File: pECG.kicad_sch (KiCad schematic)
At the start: 48 parts, among them J2 USB_C_Receptacle_USB2.0_14P, J4 AudioJack3, U2 SPX3819M5-L-3-3, U4 TP4065

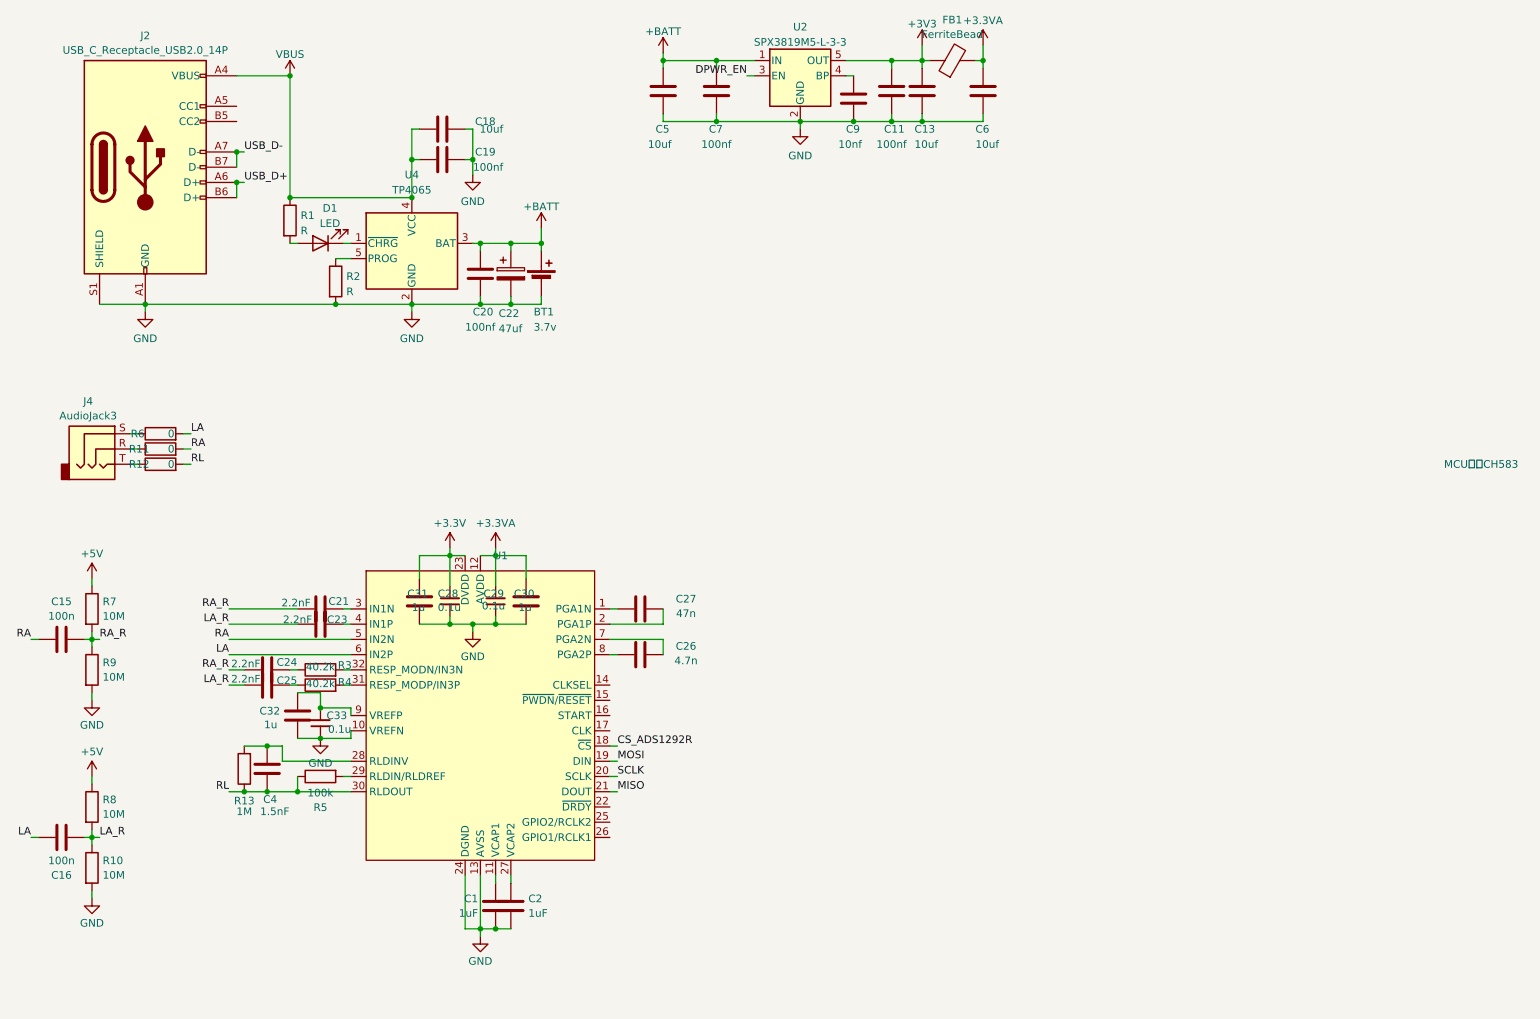
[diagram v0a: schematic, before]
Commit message: PCB部分布局和布线
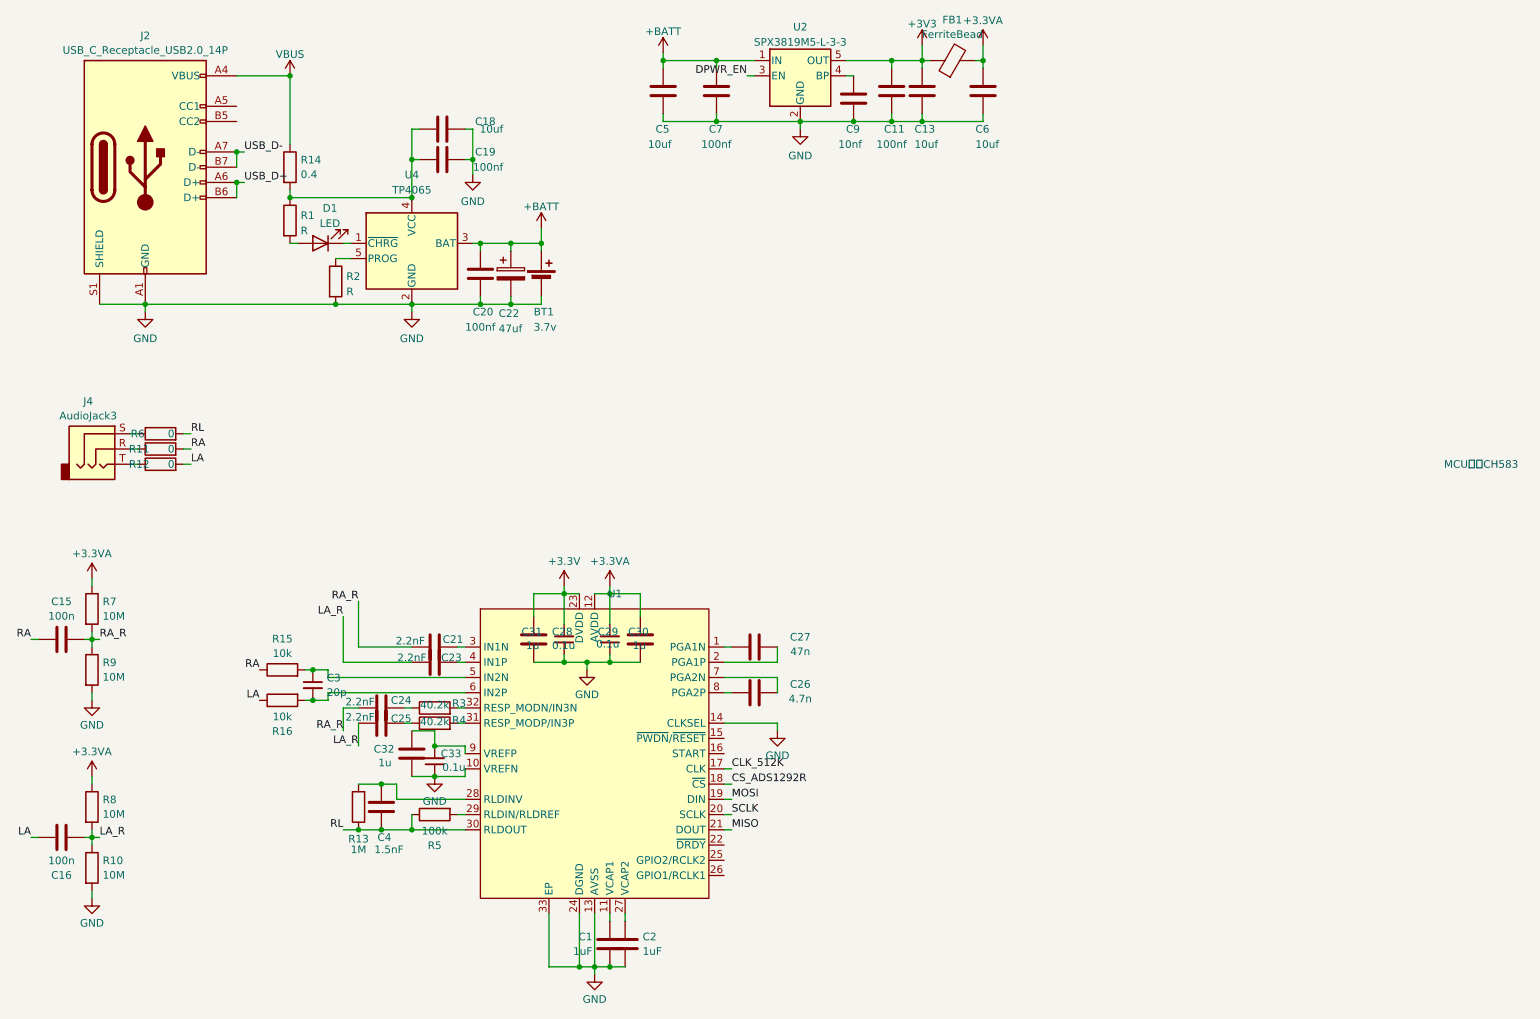
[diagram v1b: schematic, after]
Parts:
- added C3: 20p, Capacitor_SMD:C_0402_1005Metric, symbol Device:C_Small
- added R14: 0.4, Resistor_SMD:R_1206_3216Metric, symbol Device:R
- added R15, R16: 10k, Resistor_SMD:R_0402_1005Metric, symbol Device:R
- C1, C15, C16, C2, C21, C23, C24, C25, C26, C27, C29, C30, C31, C32, C4: footprint (none) -> Capacitor_SMD:C_0402_1005Metric
- C11, C19, C20, C7: footprint Capacitor_SMD:C_0603_1608Metric -> Capacitor_SMD:C_0402_1005Metric
- J2: footprint (none) -> Connector_USB:USB_C_Receptacle_Palconn_UTC16-G
- R10, R11, R12, R13, R3, R4, R5, R6, R7, R8, R9: footprint (none) -> Resistor_SMD:R_0402_1005Metric
- R2: footprint Resistor_SMD:R_0603_1608Metric -> Resistor_SMD:R_0402_1005Metric
- U1: footprint (none) -> Package_DFN_QFN:VQFN-32-1EP_4x4mm_P0.4mm_EP2.8x2.8mm_ThermalVias
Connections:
- net +5V is gone; now on net +3.3VA: R7.1, R8.1
- net GND: now also U1.14 (CLKSEL), U1.33 (EP)
- net LA: now also R12.2, R16.1; no longer R6.2, U1.6 (IN2P)
- net RA: now also R15.1; no longer U1.5 (IN2N)
- net RL: now also R6.2; no longer R12.2
- net VBUS: now also R14.1; no longer C18.1, C19.1, R1.1, U4.4 (VCC)
- net CLK_512K: now reaches U1.17 (CLK)
- new net: C3.2, R16.2, U1.6 (IN2P)
- new net: C18.1, C19.1, R1.1, R14.2, U4.4 (VCC)
- new net: C3.1, R15.2, U1.5 (IN2N)
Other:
- moved on the sheet: C1, C2, C21, C23, C24, C25, C26, C27, C28, C29, C30, C31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
